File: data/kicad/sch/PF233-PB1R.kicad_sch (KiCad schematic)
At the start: 39 parts, among them M12 12 V 1.5 A switching module, Q1A 650V SJ 95mR, Q1B 650V SJ 95mR, U1 TC4420, U3 LM393

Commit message: Transmit coil and driver (PB1R): 50 V bulk bank, 7S voltage sweep, loop-corrected on-time rule
- tx_vbus_sweep.py (make tx-vbus): TX stage over 19.6-29.4 V, reproduces sim_head1 at 26 V;
  turn-off is VBUS-independent at 20 A, Vds 456-466 V; on-time look-up table
- PB1R CD1-CD6 -> 50 V; M12 note; make pcb-pb1r; schematic export reads the generated netlist
- power_dock_check: time-domain pack/F1/CB1/cord/bank model (replaces the instant-recharge bound)
- system_budget rows for the 50 V bank, droop at the BMS cut-off, M12; regress +3 checks (36 pass)
- CORRECTIONS (lossless ton, 26 V-only stresses, droop budget, PM2 recharge model, sch source),
  ASSUMPTIONS 28-29, OPEN_ITEMS 22

Co-Authored-By: Claude Sonnet 5.5 <noreply@anthropic.com>
Claude-Session: https://claude.ai/code/session_01T7iU5pGiBfkKRBbe2JcTJx
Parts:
- CD1, CD2, CD3, CD4, CD5, CD6: value 150u 35V polymer Ta -> 150u 50V polymer Ta
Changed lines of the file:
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@@
   (symbol (lib_id "PF233_auto:CD1") (at 30.48 50.80 0) (unit 1) (exclude_from_sim no) (in_bom yes) (on_board yes) (dnp no)
     (property "Reference" "CD1" (at 30.48 48.26 0) (effects (font (size 1.27 1.27))))
-    (property "Value" "150u 35V polymer Ta" (at 30.48 54.61 0) (effects (font (size 1.0 1.0))))
+    (property "Value" "150u 50V polymer Ta" (at 30.48 54.61 0) (effects (font (size 1.0 1.0))))
     (property "Footprint" "Capacitor_Tantalum_SMD:CP_EIA-7343-43_Kemet-X" (at 30.48 50.80 0) (effects (font (size 1.27 1.27)) hide))
     (pin "1")
@@
   (symbol (lib_id "PF233_auto:CD2") (at 30.48 60.96 0) (unit 1) (exclude_from_sim no) (in_bom yes) (on_board yes) (dnp no)
     (property "Reference" "CD2" (at 30.48 58.42 0) (effects (font (size 1.27 1.27))))
-    (property "Value" "150u 35V polymer Ta" (at 30.48 64.77 0) (effects (font (size 1.0 1.0))))
+    (property "Value" "150u 50V polymer Ta" (at 30.48 64.77 0) (effects (font (size 1.0 1.0))))
     (property "Footprint" "Capacitor_Tantalum_SMD:CP_EIA-7343-43_Kemet-X" (at 30.48 60.96 0) (effects (font (size 1.27 1.27)) hide))
     (pin "1")
@@
   (symbol (lib_id "PF233_auto:CD3") (at 30.48 71.12 0) (unit 1) (exclude_from_sim no) (in_bom yes) (on_board yes) (dnp no)
     (property "Reference" "CD3" (at 30.48 68.58 0) (effects (font (size 1.27 1.27))))
-    (property "Value" "150u 35V polymer Ta" (at 30.48 74.93 0) (effects (font (size 1.0 1.0))))
+    (property "Value" "150u 50V polymer Ta" (at 30.48 74.93 0) (effects (font (size 1.0 1.0))))
     (property "Footprint" "Capacitor_Tantalum_SMD:CP_EIA-7343-43_Kemet-X" (at 30.48 71.12 0) (effects (font (size 1.27 1.27)) hide))
     (pin "1")
@@
   (symbol (lib_id "PF233_auto:CD4") (at 30.48 81.28 0) (unit 1) (exclude_from_sim no) (in_bom yes) (on_board yes) (dnp no)
     (property "Reference" "CD4" (at 30.48 78.74 0) (effects (font (size 1.27 1.27))))
-    (property "Value" "150u 35V polymer Ta" (at 30.48 85.09 0) (effects (font (size 1.0 1.0))))
+    (property "Value" "150u 50V polymer Ta" (at 30.48 85.09 0) (effects (font (size 1.0 1.0))))
     (property "Footprint" "Capacitor_Tantalum_SMD:CP_EIA-7343-43_Kemet-X" (at 30.48 81.28 0) (effects (font (size 1.27 1.27)) hide))
     (pin "1")
@@
   (symbol (lib_id "PF233_auto:CD5") (at 30.48 91.44 0) (unit 1) (exclude_from_sim no) (in_bom yes) (on_board yes) (dnp no)
     (property "Reference" "CD5" (at 30.48 88.90 0) (effects (font (size 1.27 1.27))))
-    (property "Value" "150u 35V polymer Ta" (at 30.48 95.25 0) (effects (font (size 1.0 1.0))))
+    (property "Value" "150u 50V polymer Ta" (at 30.48 95.25 0) (effects (font (size 1.0 1.0))))
     (property "Footprint" "Capacitor_Tantalum_SMD:CP_EIA-7343-43_Kemet-X" (at 30.48 91.44 0) (effects (font (size 1.27 1.27)) hide))
     (pin "1")
@@
   (symbol (lib_id "PF233_auto:CD6") (at 30.48 101.60 0) (unit 1) (exclude_from_sim no) (in_bom yes) (on_board yes) (dnp no)
     (property "Reference" "CD6" (at 30.48 99.06 0) (effects (font (size 1.27 1.27))))
-    (property "Value" "150u 35V polymer Ta" (at 30.48 105.41 0) (effects (font (size 1.0 1.0))))
+    (property "Value" "150u 50V polymer Ta" (at 30.48 105.41 0) (effects (font (size 1.0 1.0))))
     (property "Footprint" "Capacitor_Tantalum_SMD:CP_EIA-7343-43_Kemet-X" (at 30.48 101.60 0) (effects (font (size 1.27 1.27)) hide))
     (pin "1")

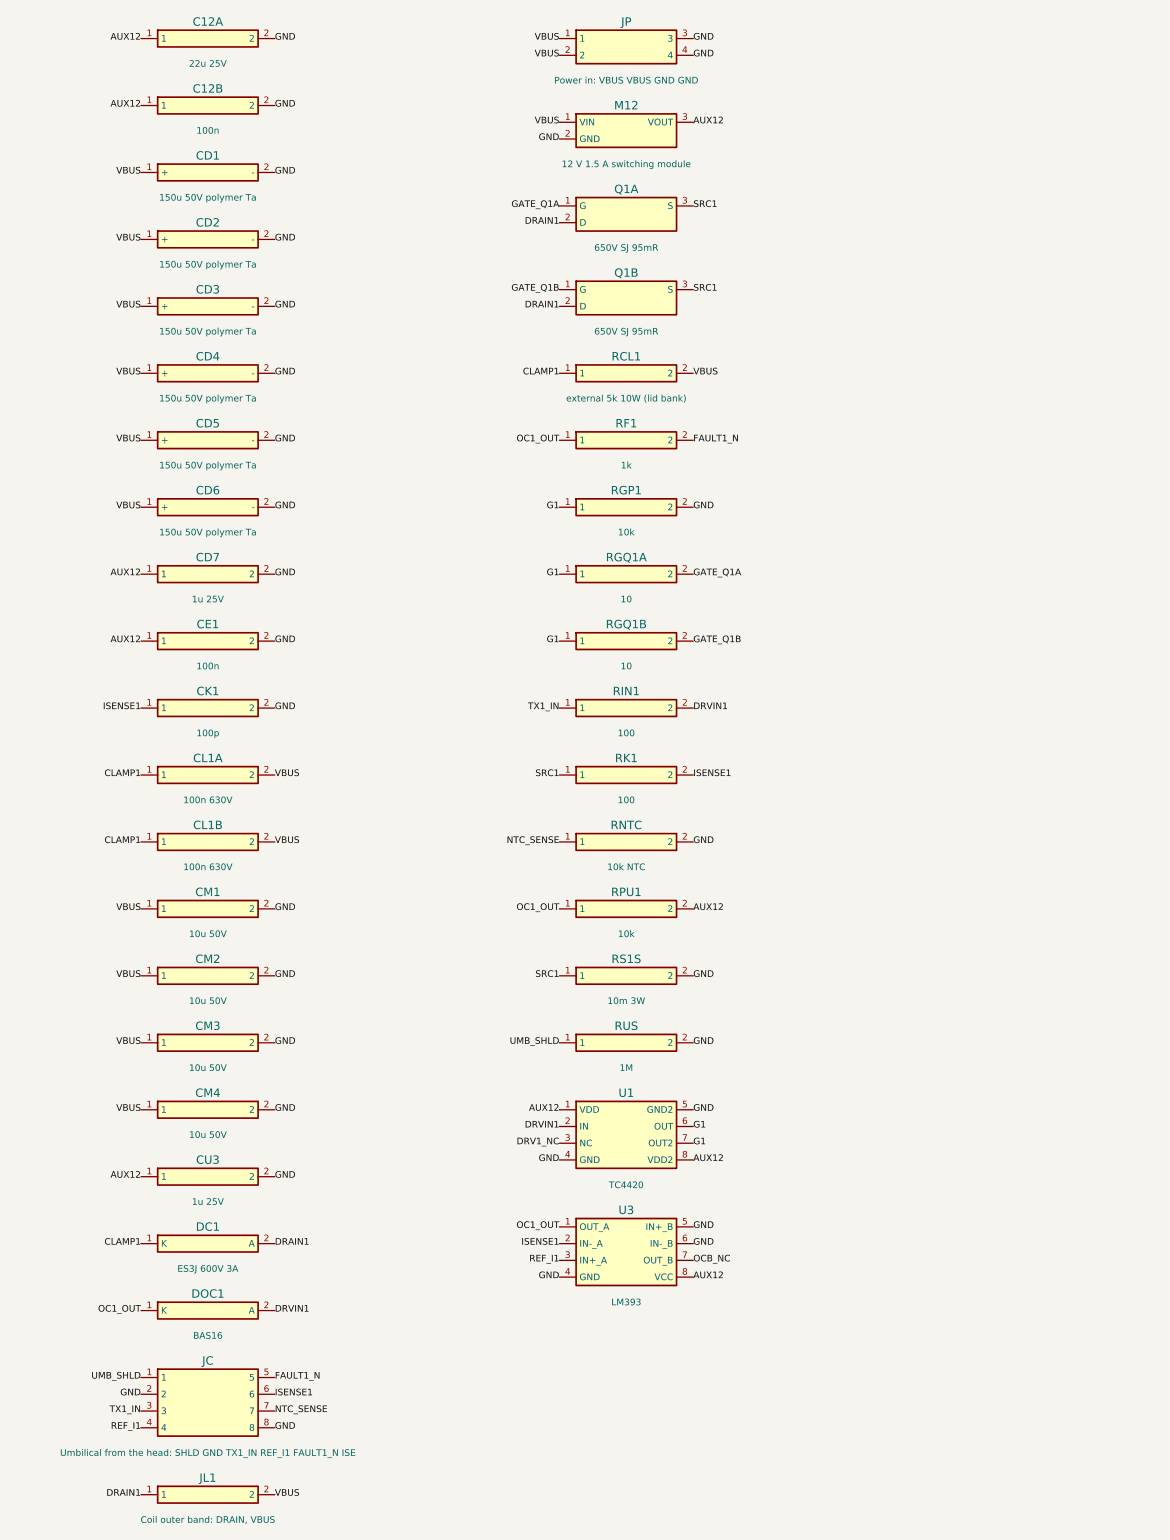
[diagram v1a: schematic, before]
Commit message: Step 5: datasheets and fabricator sheets (vendor-derived floor, verified parts, PB1R 9-can bank, Gerber edge read-back)
- Fab floor from AdvancedPCB / TTM pages (docs/design/FAB_RULES_VERIFIED.md, U-FAB-RULES closed): clearance 0.16,
  component-PTH ring 0.18 / hole 0.46, drill-copper 0.26, drill-drill 0.41, every rule (severity error).
  CB1D JA/JB and HB2 TO-92 pads 1.02 mm; route_fix merges close same-net vias (CB1D, LB1).
- Parts from manufacturer PDFs (docs/design/DATASHEET_LOG.md): PB1R bulk 9 x Panasonic EEHZC1H101P
  (the 150 uF / 50 V polymer-Ta was not found; bank stays 900 uF, on-time table unchanged), PB1R re-placed
  with the Kelvin/comparator cluster pinned (pulse path 4.9 mohm, spike 7.5 V, ground ref 15.5 mV unchanged);
  SMCJ30A (SMCJ33A clamps 53.3 V > 50 V parts), Si4401FDY, BZT52C15, Bourns SF-1206S500-2 (new 1206 land),
  DRV5023BIQLPG, CRCW2512 500 V, OPA2365/OPA2211/LM393/CD74HC4051 checked. ES3J 600 V kept as a WATCH.
- U-DS-PARTS split into groups; open: TXDRIVE, OKI, PACK, BAV199, HVTERM. U-COLD-BOOTSTRAP closed.
- Controls retargeted to fixture folders (12/12). Netlist date fixed (data changed daily).
- Gerber planes from gerber_out.py ran into the notch and to 0.1 mm of the edge since r1 (found by the
  independent review): fixed, and gerber_edge_check.py reads every copper layer back.
- New Gerber sets CB1D_B3, LB1_v5, PB1R_v2; old sets marked SUPERSEDED.
- Findings for the owner: aluminium cans ~0.5 x a 1 g nugget (OPEN_ITEMS 34), OPA2365 capacitive load (30),
  OPA2211 input range on 5 V (31), Hall magnet spread (32).
- Strict regress 55 PASS / 0 FAIL / 0 SKIP; sign-off 44 PASS / 0 FAIL / 0 SKIP / 19 UNVERIFIED.

Co-Authored-By: Claude Opus 5.5 <noreply@anthropic.com>
Claude-Session: https://claude.ai/code/session_015VKhZtgEAWnezB2NDY75VV
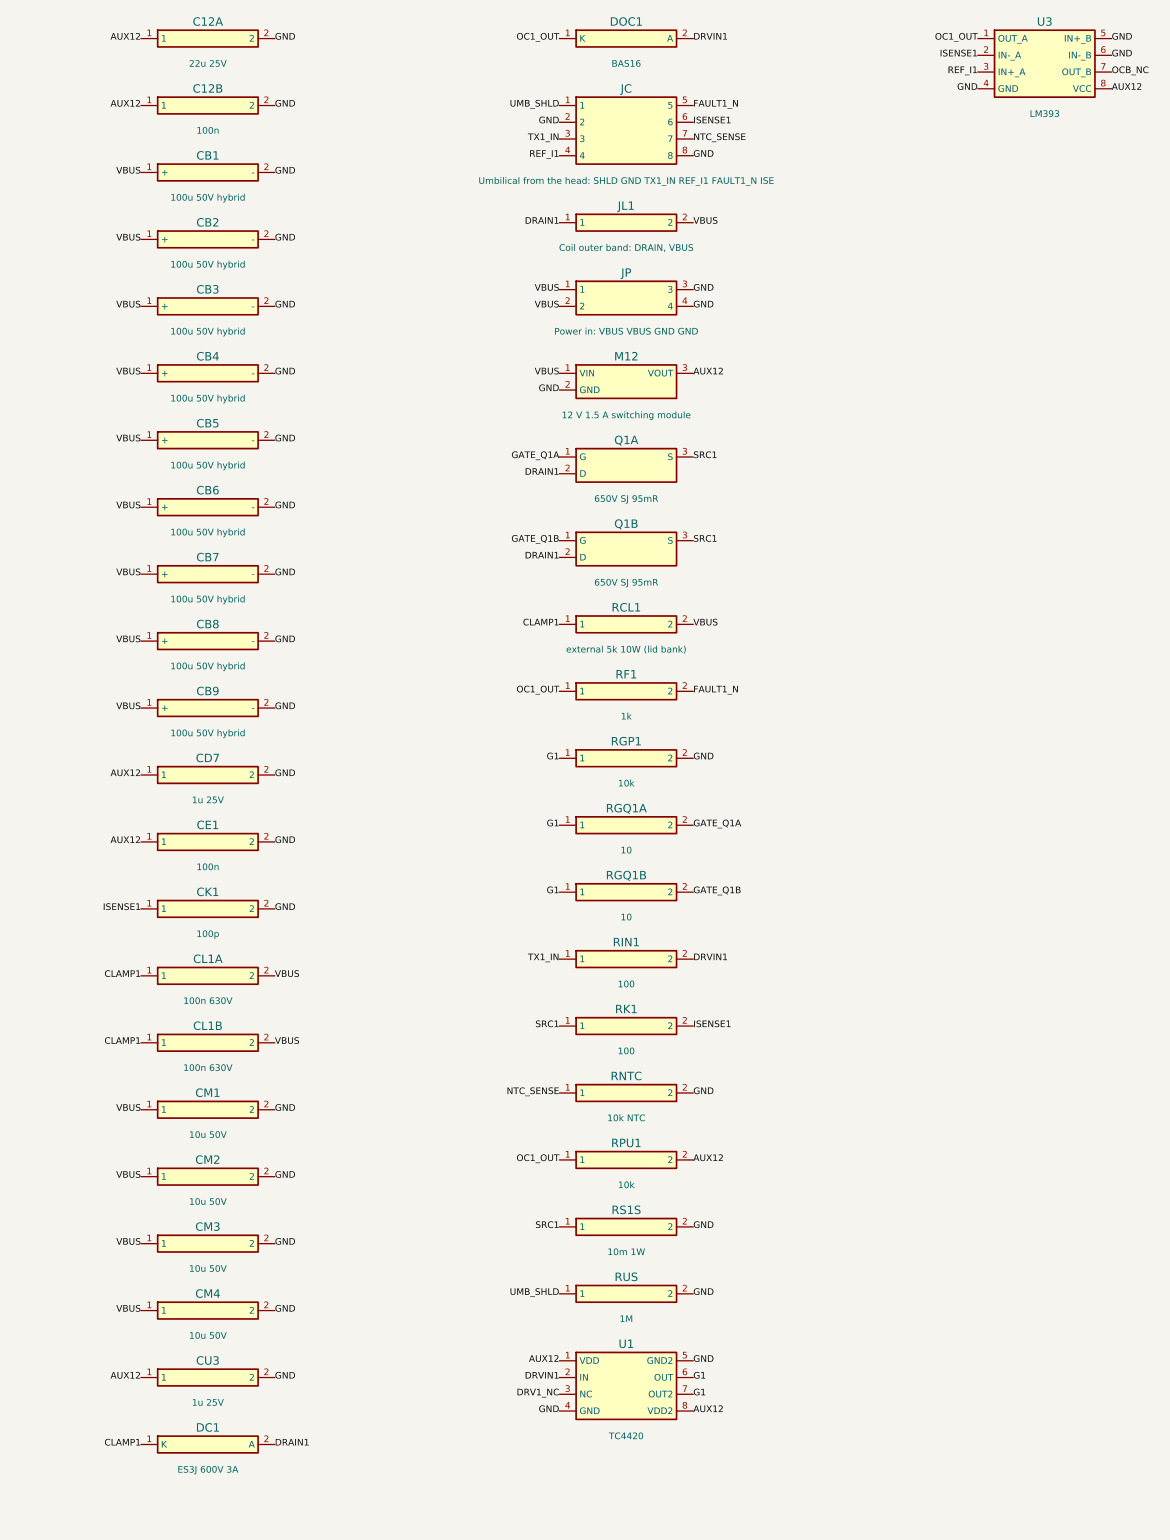
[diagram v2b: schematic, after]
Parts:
- removed CD1: 150u 50V polymer Ta, Capacitor_Tantalum_SMD:CP_EIA-7343-43_Kemet-X, symbol PF233_auto:CD1
- removed CD2: 150u 50V polymer Ta, Capacitor_Tantalum_SMD:CP_EIA-7343-43_Kemet-X, symbol PF233_auto:CD2
- removed CD3: 150u 50V polymer Ta, Capacitor_Tantalum_SMD:CP_EIA-7343-43_Kemet-X, symbol PF233_auto:CD3
- removed CD4: 150u 50V polymer Ta, Capacitor_Tantalum_SMD:CP_EIA-7343-43_Kemet-X, symbol PF233_auto:CD4
- removed CD5: 150u 50V polymer Ta, Capacitor_Tantalum_SMD:CP_EIA-7343-43_Kemet-X, symbol PF233_auto:CD5
- removed CD6: 150u 50V polymer Ta, Capacitor_Tantalum_SMD:CP_EIA-7343-43_Kemet-X, symbol PF233_auto:CD6
- added CB1: 100u 50V hybrid, Capacitor_SMD:CP_Elec_10x10, symbol PF233_auto:CB1
- added CB2: 100u 50V hybrid, Capacitor_SMD:CP_Elec_10x10, symbol PF233_auto:CB2
- added CB3: 100u 50V hybrid, Capacitor_SMD:CP_Elec_10x10, symbol PF233_auto:CB3
- added CB4: 100u 50V hybrid, Capacitor_SMD:CP_Elec_10x10, symbol PF233_auto:CB4
- added CB5: 100u 50V hybrid, Capacitor_SMD:CP_Elec_10x10, symbol PF233_auto:CB5
- added CB6: 100u 50V hybrid, Capacitor_SMD:CP_Elec_10x10, symbol PF233_auto:CB6
- added CB7: 100u 50V hybrid, Capacitor_SMD:CP_Elec_10x10, symbol PF233_auto:CB7
- added CB8: 100u 50V hybrid, Capacitor_SMD:CP_Elec_10x10, symbol PF233_auto:CB8
- added CB9: 100u 50V hybrid, Capacitor_SMD:CP_Elec_10x10, symbol PF233_auto:CB9
- RS1S: value 10m 3W -> 10m 1W
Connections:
- net GND: now also CB1.2 (-), CB2.2 (-), CB3.2 (-), CB4.2 (-), CB5.2 (-), CB6.2 (-), CB7.2 (-), CB8.2 (-), CB9.2 (-)
- net VBUS: now also CB1.1 (+), CB2.1 (+), CB3.1 (+), CB4.1 (+), CB5.1 (+), CB6.1 (+), CB7.1 (+), CB8.1 (+), CB9.1 (+)
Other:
- moved on the sheet: CD7, CE1, CK1, CL1A, CL1B, CM1, CM2, CM3, CM4, CU3, DC1, DOC1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

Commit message: WIP stage 5: B3/B5/B6/B8 closed in blockers.json, B7 narrowed to HVTERM, B12 opened; cap-v18 pipeline step (cap was not regenerated on a fresh work/); upper_check septum joint by voxels; curated STLs refreshed (U6 dock for the real MT60, septum lap segments, canonical face order); DESIGN_STATE stress counts
Co-Authored-By: Claude Opus 5.5 <noreply@anthropic.com>
Claude-Session: https://claude.ai/code/session_01FX4DWSYYjMCFGGA6gmha65
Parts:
- M12: value 12 V 1.5 A switching module -> 12 V 1.0 A switching module
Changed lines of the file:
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@@
   (symbol (lib_id "PF233_auto:M12") (at 93.98 81.28 0) (unit 1) (exclude_from_sim no) (in_bom yes) (on_board yes) (dnp no)
     (property "Reference" "M12" (at 93.98 78.74 0) (effects (font (size 1.27 1.27))))
-    (property "Value" "12 V 1.5 A switching module" (at 93.98 87.63 0) (effects (font (size 1.0 1.0))))
+    (property "Value" "12 V 1.0 A switching module" (at 93.98 87.63 0) (effects (font (size 1.0 1.0))))
     (property "Footprint" "Converter_DCDC:Converter_DCDC_Murata_OKI-78SR_Horizontal" (at 93.98 81.28 0) (effects (font (size 1.27 1.27)) hide))
     (pin "1")

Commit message: WIP (NOT signed off): data published by the second close-out run (8 FAIL: 3 opens on CB1D-C2 / AU1 under the exact fine-zone keep-out); third run in progress
Co-Authored-By: Claude Opus 5.5 <noreply@anthropic.com>
Claude-Session: https://claude.ai/code/session_01FX4DWSYYjMCFGGA6gmha65
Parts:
- JL1: value Coil outer band: DRAIN, VBUS -> Coil pair: DRAIN1, VBUS (AWG12 soldered); footprint Connector:Terminal_block_1x2_P5.08mm -> Connector:Solder_holes_AWG12_1x2_P5.08mm
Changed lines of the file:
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@@
   (symbol (lib_id "PF233_auto:JL1") (at 93.98 58.42 0) (unit 1) (exclude_from_sim no) (in_bom yes) (on_board yes) (dnp no)
     (property "Reference" "JL1" (at 93.98 55.88 0) (effects (font (size 1.27 1.27))))
-    (property "Value" "Coil outer band: DRAIN, VBUS" (at 93.98 62.23 0) (effects (font (size 1.0 1.0))))
-    (property "Footprint" "Connector:Terminal_block_1x2_P5.08mm" (at 93.98 58.42 0) (effects (font (size 1.27 1.27)) hide))
+    (property "Value" "Coil pair: DRAIN1, VBUS (AWG12 soldered)" (at 93.98 62.23 0) (effects (font (size 1.0 1.0))))
+    (property "Footprint" "Connector:Solder_holes_AWG12_1x2_P5.08mm" (at 93.98 58.42 0) (effects (font (size 1.27 1.27)) hide))
     (pin "1")
     (pin "2")

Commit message: Close-out of the output modes / audio / gyro integration: sign-off 76 PASS / 0 FAIL / 4 UNVERIFIED, strict regress 114 / 0, release controls 12 / 12, publish 0 stale
AU1 (36 x 60, 8 layers, gyro moved from CB1D) routed 38 / 38, CB1D-C2 46 / 46, both exact DRC 0 / 0; PB1R-v5 AWG12 solder holes; PM2-B, HB2-B; superseded Gerber sets marked.
Tooling now default: exact-geometry DRC, router fine-pitch keep-out / neck-down / per-board grid, local repair, round checkpoints, non-destructive reset,
interface check, AU1 3-D models with gull-wing leads, counted HV check; pad check traced by the pipeline; process-guard regress row; PROCESS.md / CLAUDE.md / handoff updated.

Co-Authored-By: Claude Opus 5.5 <noreply@anthropic.com>
Claude-Session: https://claude.ai/code/session_01FX4DWSYYjMCFGGA6gmha65
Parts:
- JC: footprint Connector:Pin_header_2x4_P2.54mm -> Connector:Wire_pads_2x4_P2.54mm
- JL1: footprint Connector:Solder_holes_AWG12_1x2_P5.08mm -> Connector:Wire_pads_AWG12_1x2_P5.08mm
- JP: footprint Connector:Terminal_block_1x4_P5.08mm -> Connector:Wire_pads_1x4_P5.08mm
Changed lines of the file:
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@@
     (property "Reference" "JC" (at 93.98 38.10 0) (effects (font (size 1.27 1.27))))
     (property "Value" "Umbilical from the head: SHLD GND TX1_IN REF_I1 FAULT1_N ISE" (at 93.98 52.07 0) (effects (font (size 1.0 1.0))))
-    (property "Footprint" "Connector:Pin_header_2x4_P2.54mm" (at 93.98 40.64 0) (effects (font (size 1.27 1.27)) hide))
+    (property "Footprint" "Connector:Wire_pads_2x4_P2.54mm" (at 93.98 40.64 0) (effects (font (size 1.27 1.27)) hide))
     (pin "1")
     (pin "2")
@@
     (property "Reference" "JL1" (at 93.98 55.88 0) (effects (font (size 1.27 1.27))))
     (property "Value" "Coil pair: DRAIN1, VBUS (AWG12 soldered)" (at 93.98 62.23 0) (effects (font (size 1.0 1.0))))
-    (property "Footprint" "Connector:Solder_holes_AWG12_1x2_P5.08mm" (at 93.98 58.42 0) (effects (font (size 1.27 1.27)) hide))
+    (property "Footprint" "Connector:Wire_pads_AWG12_1x2_P5.08mm" (at 93.98 58.42 0) (effects (font (size 1.27 1.27)) hide))
     (pin "1")
     (pin "2")
@@
     (property "Reference" "JP" (at 93.98 66.04 0) (effects (font (size 1.27 1.27))))
     (property "Value" "Power in: VBUS VBUS GND GND" (at 93.98 74.93 0) (effects (font (size 1.0 1.0))))
-    (property "Footprint" "Connector:Terminal_block_1x4_P5.08mm" (at 93.98 68.58 0) (effects (font (size 1.27 1.27)) hide))
+    (property "Footprint" "Connector:Wire_pads_1x4_P5.08mm" (at 93.98 68.58 0) (effects (font (size 1.27 1.27)) hide))
     (pin "1")
     (pin "2")

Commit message: WIP: published PB1R KiCad / schematic outputs and pipeline graph for the B7 close-out (sign-off re-run pending)
Co-Authored-By: Claude Opus 5.5 <noreply@anthropic.com>
Claude-Session: https://claude.ai/code/session_01FX4DWSYYjMCFGGA6gmha65
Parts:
- RCL1: value external 5k 10W (lid bank) -> 4 x Vishay PR03 1K24 1% 750V 3W in series, 4.96k, NPM hot zo
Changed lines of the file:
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@@
   (symbol (lib_id "PF233_auto:RCL1") (at 93.98 119.38 0) (unit 1) (exclude_from_sim no) (in_bom yes) (on_board yes) (dnp no)
     (property "Reference" "RCL1" (at 93.98 116.84 0) (effects (font (size 1.27 1.27))))
-    (property "Value" "external 5k 10W (lid bank)" (at 93.98 123.19 0) (effects (font (size 1.0 1.0))))
+    (property "Value" "4 x Vishay PR03 1K24 1% 750V 3W in series, 4.96k, NPM hot zo" (at 93.98 123.19 0) (effects (font (size 1.0 1.0))))
     (property "Footprint" "Connector:SolderPad_2x_P5.08mm" (at 93.98 119.38 0) (effects (font (size 1.27 1.27)) hide))
     (pin "1")

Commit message: Speed-up: batched Gerber geometry (10x, same copper) and parallel sign-off controls (245 s -> 32 s); B7 sign-off run
gerber_geom.layer_geometry merges same-polarity runs with unary_union (worst sym-diff 6e-13 mm2
over 258 layers; regress row keeps the sequential build as reference). publish 79 -> 10.5 s.
release_signoff_controls runs independent jobs in a thread pool, stale-data control alone last.
Sign-off 77 PASS / 0 FAIL / 3 UNVERIFIED, strict regress 120 / 0, publish 0 stale.
Moved: US3M diode margins (reverse voltage 27.5 -> 56.5 %, current 80.1 -> 83.4 %).

Co-Authored-By: Claude Opus 5.5 <noreply@anthropic.com>
Claude-Session: https://claude.ai/code/session_01FX4DWSYYjMCFGGA6gmha65
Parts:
- DC1: value ES3J 600V 3A -> US3M 1000V 3A
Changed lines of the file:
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@@
   (symbol (lib_id "PF233_auto:DC1") (at 30.48 243.84 0) (unit 1) (exclude_from_sim no) (in_bom yes) (on_board yes) (dnp no)
     (property "Reference" "DC1" (at 30.48 241.30 0) (effects (font (size 1.27 1.27))))
-    (property "Value" "ES3J 600V 3A" (at 30.48 247.65 0) (effects (font (size 1.0 1.0))))
+    (property "Value" "US3M 1000V 3A" (at 30.48 247.65 0) (effects (font (size 1.0 1.0))))
     (property "Footprint" "Diode_SMD:D_SMC" (at 30.48 243.84 0) (effects (font (size 1.27 1.27)) hide))
     (pin "1")
